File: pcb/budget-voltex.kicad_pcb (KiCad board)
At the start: 2 copper layers, 10 parts

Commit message: finish schematic, finish wiring for pcb
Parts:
- added R1: 5K1, Resistor_SMD:R_0603_1608Metric_Pad0.98x0.95mm_HandSolder, F.Cu at (137.5, 102.6)
- added R2: 5K1, Resistor_SMD:R_0603_1608Metric_Pad0.98x0.95mm_HandSolder, F.Cu at (135.6, 102.6)
- added R3: 5K1, Resistor_SMD:R_0603_1608Metric_Pad0.98x0.95mm_HandSolder, F.Cu at (157.3, 40.4)
- added R4: 5K1, Resistor_SMD:R_0603_1608Metric_Pad0.98x0.95mm_HandSolder, F.Cu at (145.4, 40.3)
- added USB1: HRO-TYPE-C-31-M-12, Type-C:HRO-TYPE-C-31-M-12-HandSoldering, F.Cu at (151.5, 31.3)
- A1: footprint Module:RaspberryPi_Pico_SMD_HandSolder -> Module:RaspberryPi_Pico_SMD
- moved KnobR1 72.5 mm to (51.4, 48.1), turned to 180 degrees
- moved A1 66.8 mm to (151.9, 127.4)
- moved KnobL1 57.2 mm to (251.9, 48.1)
- moved BT-D1 50.7 mm to (221.7, 78.8)
- moved BT-A1 46.3 mm to (86.7, 78.8)
- moved BT-C1 35.2 mm to (176.7, 78.7)
- moved BT-B1 34.3 mm to (131.7, 78.8)
- moved FX-L1 28.7 mm to (199.2, 138.8)
- moved Start1 26.5 mm to (154.2, 43.0)
- moved FX-R1 18.8 mm to (109.2, 138.8)
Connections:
- A1 pad 36: unconnected-(A1-3V3-Pad36) -> +3V3
- A1 pad 40: unconnected-(A1-VBUS-Pad40) -> Net-(A1-VBUS)
- BT-A1 pad 2: Net-(BT-A1-B) -> GND
- BT-B1 pad 2: Net-(BT-A1-B) -> GND
- BT-C1 pad 2: Net-(BT-A1-B) -> GND
- BT-D1 pad 2: Net-(BT-A1-B) -> GND
- FX-L1 pad 2: Net-(BT-A1-B) -> GND
- FX-R1 pad 2: Net-(BT-A1-B) -> GND
- Start1 pad 2: Net-(BT-A1-B) -> GND
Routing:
- net GND: track 0.00 -> 501.7 mm
- net SCL: track 0.00 -> 301.5 mm, vias 0 -> 6
- net SDA: track 0.00 -> 290.6 mm, vias 0 -> 2
- net Net-(A1-GPIO12): track 0.00 -> 151.5 mm
- net Net-(A1-GPIO11): track 0.00 -> 135.1 mm
- net Net-(A1-GPIO6): track 0.00 -> 119.8 mm, vias 0 -> 2
- net Net-(A1-VBUS): track 0.00 -> 83.9 mm, vias 0 -> 6
- net Net-(A1-GPIO4): track 0.00 -> 81.6 mm, vias 0 -> 2
- net Net-(A1-GPIO7): track 0.00 -> 80.1 mm, vias 0 -> 2
- net Net-(A1-GPIO9): track 0.00 -> 77.3 mm
- net Net-(A1-USB_DM): track 0.00 -> 72.4 mm, vias 0 -> 1
- net Net-(A1-USB_DP): track 0.00 -> 72.0 mm, vias 0 -> 1
- net Net-(A1-GPIO10): track 0.00 -> 58.0 mm, vias 0 -> 1
- net Net-(A1-GPIO8): track 0.00 -> 54.4 mm, vias 0 -> 2
- net +3V3: track 0.00 -> 49.6 mm
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
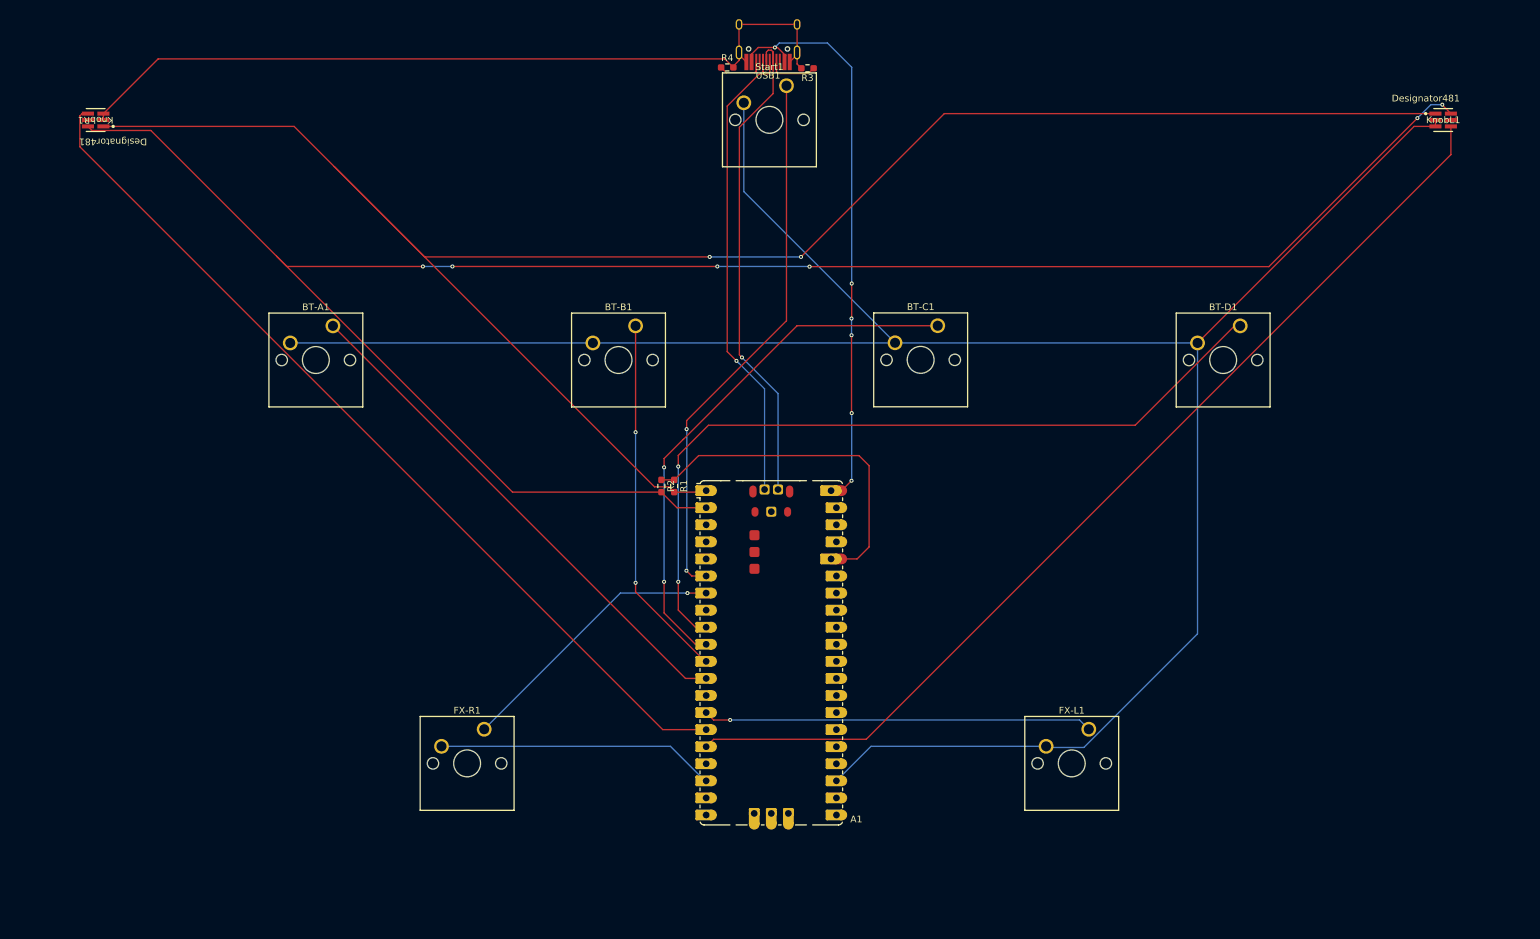
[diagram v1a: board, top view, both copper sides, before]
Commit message: update wiring/schematic, shape pcb
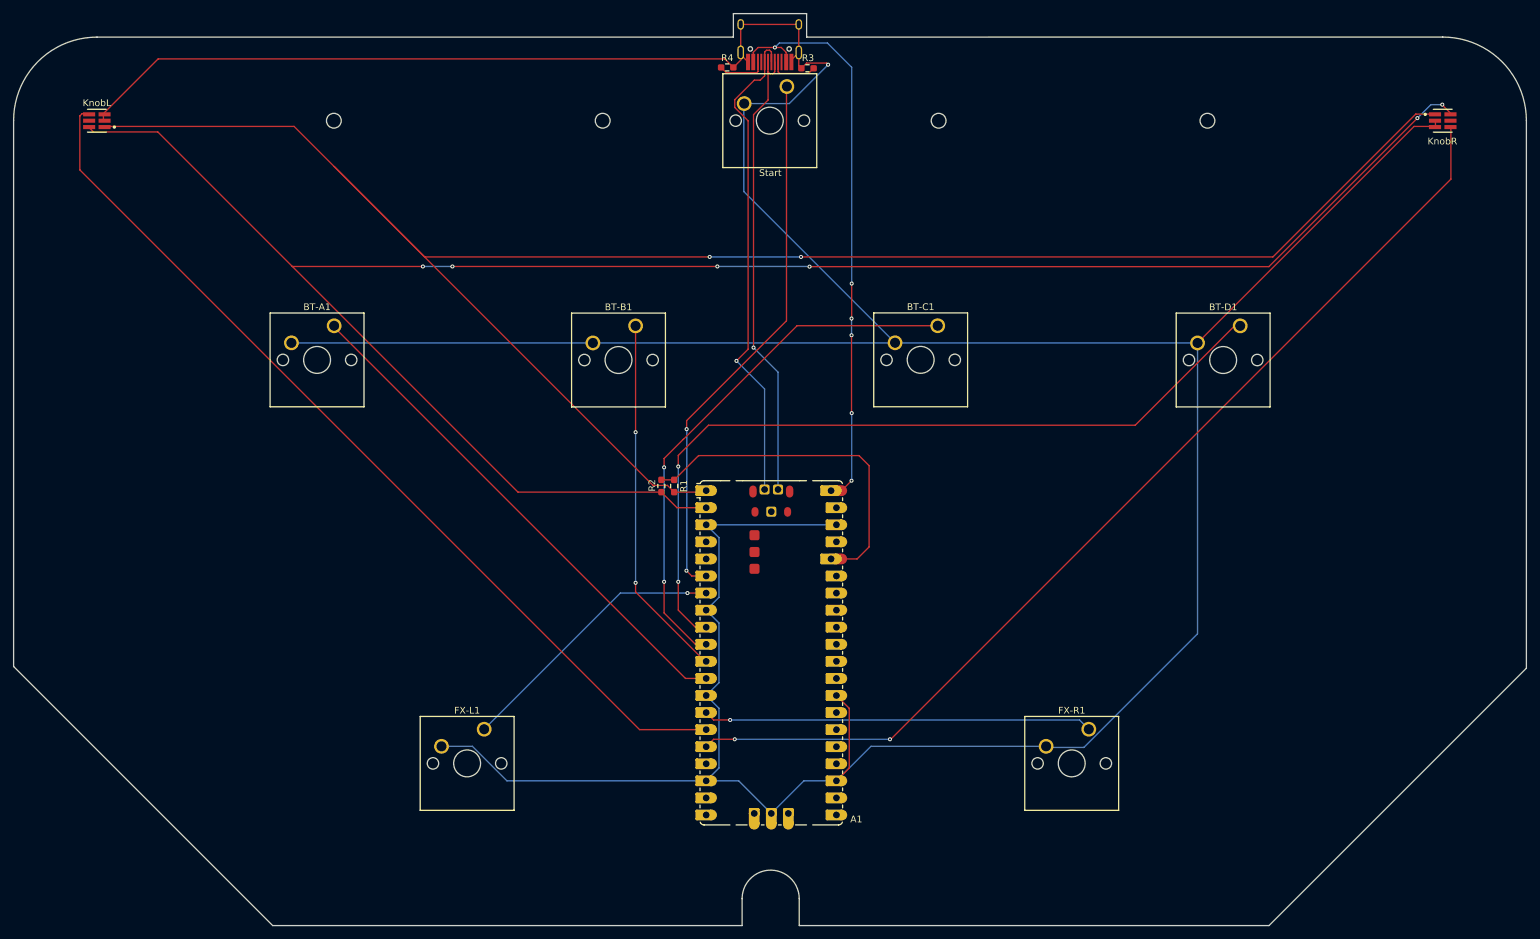
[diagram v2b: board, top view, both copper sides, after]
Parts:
- added REF**: MountingHole_2.2mm_M2, MountingHole:MountingHole_2.2mm_M2, F.Cu at (176.8, 48.2)
- added REF**: MountingHole_2.2mm_M2, MountingHole:MountingHole_2.2mm_M2, F.Cu at (86.9, 48.2)
- added REF**: MountingHole_2.2mm_M2, MountingHole:MountingHole_2.2mm_M2, F.Cu at (126.9, 48.2)
- added REF**: MountingHole_2.2mm_M2, MountingHole:MountingHole_2.2mm_M2, F.Cu at (216.8, 48.2)
- moved USB1 0.25 mm to (151.7, 31.3)
- moved KnobL 0.21 mm to (51.6, 48.2)
- moved BT-A1 0.18 mm to (86.9, 78.8)
- moved Start 0.13 mm to (154.3, 43.1)
- moved KnobR 0.12 mm to (251.9, 48.2)
- renumbered FX-R1 to FX-L1, FX-L1 to FX-R1, KnobR1 to KnobL, KnobL1 to KnobR, Start1 to Start
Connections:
- A1 pad : (no net) -> +3V3
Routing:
- net GND: track 501.7 -> 620.9 mm, vias 0 -> 1
- net Net-(A1-USB_DM): track 72.4 -> 68.7 mm
- net SCL: track 301.5 -> 298.5 mm
- net Net-(A1-GPIO12): track 151.5 -> 153.6 mm, vias 0 -> 2
- net Net-(A1-GPIO11): track 135.1 -> 137.1 mm
- net Net-(A1-USB_DP): track 72.0 -> 73.4 mm
- net Net-(A1-VBUS): track 83.9 -> 85.1 mm
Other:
- board outline added: 225.1 x 135.7 mm
